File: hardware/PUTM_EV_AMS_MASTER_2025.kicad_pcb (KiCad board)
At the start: 4 copper layers, 60 x 100 mm, 261 parts, among them IC1 TPS7B92033DBVR, IC11 ISO6760, IC2 TPS54202HDDCR, IC3 BQ79600PWRQ1, IC4 ADS131M04, IC5 LTC1799, IC6 LTC6820IMS, IC7 ISO6760, IC8 3.3V/0.5A, J1 M80-5100642, J10 M300-MV10345M1, J12 M80-51034XX, J2 USB_C_Receptacle_USB2.0_14P, J3 M80-51014XX, J4 FTSH-107-01-L-D-K, J5 M80-51004XX, J7 M300-MV10345M1, J8 M80-51004XX, K1 IMB03ITS, Q1 DMT6018LDR-7, Q2 DMT6018LDR-7, Q3 DMT6018LDR-7, Q4 DMT6018LDR-7, Q5 DMT6018LDR-7, Q6 2N7002, Q7 DMT6018LDR-7, Q8 2N7002, Q9 2N7002, T1 >100kHz, U1 MCP2542FD-E/MF, U10 STM32G484VEHx, U11 LM397, U12 LMR33640DDDA, U2 LM397, U3 74AUP1G32, U4 UCC12040DVE, U5 LM397, U6 MCP2542FD-E/MF, U7 MCP2542FD-E/MF, U8 LM397, U9 LM397, Y1 X322516MLB4SI

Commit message: sync
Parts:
- removed C76: 10nF, Capacitor_SMD:C_0603_1608Metric
- removed C77: 100nF, Capacitor_SMD:C_0603_1608Metric
- removed R84, R85, R86, R87: 10k, Resistor_SMD:R_0603_1608Metric
- removed R88, R89, R90: TBD, Resistor_SMD:R_0603_1608Metric
- removed U11: LM397, Package_TO_SOT_SMD:SOT-23-5
- added C81: 100nF, Capacitor_SMD:C_0603_1608Metric, F.Cu at (191.2, 34.4)
- added C82: 100nF, Capacitor_SMD:C_0603_1608Metric, F.Cu at (191.2, 36.9)
- added R100: 100, Resistor_SMD:R_0603_1608Metric, F.Cu at (202.3, 34.4)
- added R101: 10k, Resistor_SMD:R_0603_1608Metric, F.Cu at (191.2, 39.4)
- added R102: 10k, Resistor_SMD:R_0603_1608Metric, F.Cu at (191.2, 42.0)
- added R103: 10k, Resistor_SMD:R_0603_1608Metric, F.Cu at (191.2, 44.5)
- added R104: 10k, Resistor_SMD:R_0603_1608Metric, F.Cu at (191.2, 47.0)
- added R105: TBD, Resistor_SMD:R_0603_1608Metric, F.Cu at (191.2, 49.5)
- added R106: TBD, Resistor_SMD:R_0603_1608Metric, F.Cu at (191.2, 52.0)
- added R107: TBD, Resistor_SMD:R_0603_1608Metric, F.Cu at (191.2, 54.5)
- added U13: LM397, Package_TO_SOT_SMD:SOT-23-5, F.Cu at (195.8, 35.6)
- C5, C72, C74: value 10nF -> 100nF
- IC4: value ADS131M04 -> ~
- R38: value 10k -> TBD
- R42: value TBD -> 10k
- moved C74 10.1 mm to (181.5, 116.5)
- moved C75 10.1 mm to (178.5, 121.0)
- moved R77 10.1 mm to (178.5, 116.5)
- moved R78 10.1 mm to (178.5, 119.5)
- moved R79 10.1 mm to (178.5, 115.0)
- moved R80 10.1 mm to (178.5, 118.0)
- moved R81 10.1 mm to (181.5, 118.0)
- moved R82 10.1 mm to (181.5, 119.5)
- moved R83 10.1 mm to (181.5, 121.0)
- moved U9 10.1 mm to (180.0, 118.0)
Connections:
- net /Connectivity/EAAE renamed /Connectivity/AIR Minus/EI1
- net /Connectivity/EAAM renamed /Connectivity/AIR Plus/EI1
- C5 pad 1: /Connectivity/EI2 -> /Connectivity/Input2/EI1
- C50 pad 1: /Connectivity/EI1 -> +24V
- C66 pad 1: +24V -> /Connectivity/AIR Precharge/EI1
- Q6 pad 1: /MCU/SIGNAL_AMS_ERROR -> Net-(Q6-G)
- R11 pad 1: /MCU/SIGNAL_AMS_ERROR -> Net-(Q6-G)
- R33 pad 1: /Connectivity/EI2 -> +24V
- R33 pad 2: /CHARGER_DETECTION -> /Connectivity/Input2/EI1
- R35 pad 1: /Connectivity/EI2 -> /Connectivity/Input2/EI1
- R38 pad 1: +3.3V -> /Connectivity/Input2/EI1
- R38 pad 2: /Connectivity/UC_IN1 -> /CHARGER_DETECTION
- R39 pad 1: Net-(R39-Pad1) -> +3.3V
- R39 pad 2: /Connectivity/UC_IN1 -> /AIR_PRE_DETECTION
- R40 pad 1: +3.3V -> Net-(R40-Pad1)
- R40 pad 2: Net-(R39-Pad1) -> /AIR_PRE_DETECTION
- R41 pad 1: Net-(R39-Pad1) -> +3.3V
- R41 pad 2: GND -> Net-(R40-Pad1)
- R42 pad 1: /Connectivity/EI1 -> Net-(R40-Pad1)
- R42 pad 2: TSMS -> GND
- R43 pad 1: /Connectivity/EI1 -> +24V
- R43 pad 2: GND -> /Connectivity/AIR Precharge/EI1
- R68 pad 1: +24V -> /Connectivity/AIR Precharge/EI1
- R68 pad 2: /Connectivity/EI1 -> GND
- R69 pad 1: +24V -> /Connectivity/AIR Precharge/EI1
- R69 pad 2: /Connectivity/EI2 -> /Connectivity/EX_AIR_AUX_PRE
- R70 pad 2: /AIR_PRE_DETECTION -> /Connectivity/UC_AIR_AUX_M
- R71 pad 2: /AIR_PRE_DETECTION -> /Connectivity/UC_AIR_AUX_M
- R76 pad 2: /Connectivity/EX_AIR_AUX_PRE -> /AIR_M_DETECTION
- R77 pad 2: /Connectivity/UC_AIR_AUX_M -> /Connectivity/UC_AIR_AUX_P
- R78 pad 2: /Connectivity/UC_AIR_AUX_M -> /Connectivity/UC_AIR_AUX_P
- R83 pad 2: /AIR_M_DETECTION -> /AIR_P_DETECTION
- U2 pad 3: /Connectivity/EI2 -> /Connectivity/Input2/EI1
- U5 pad 1: Net-(R39-Pad1) -> Net-(R40-Pad1)
- U5 pad 3: /Connectivity/EI1 -> /Connectivity/AIR Precharge/EI1
- U5 pad 4: /Connectivity/UC_IN1 -> /AIR_PRE_DETECTION
- U8 pad 4: /AIR_PRE_DETECTION -> /Connectivity/UC_AIR_AUX_M
- U9 pad 4: /Connectivity/UC_AIR_AUX_M -> /Connectivity/UC_AIR_AUX_P
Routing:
- net (no net): track 0.00 -> 29.1 mm
- net +24V: track 12.7 -> 4.34 mm, vias 5 -> 0
- net Net-(R39-Pad1): track 7.43 -> 0.00 mm, vias 1 -> 0
- net Net-(R85-Pad1): track 7.43 -> 0.00 mm, vias 1 -> 0
- net /Connectivity/EI1: track 6.79 -> 0.00 mm, vias 1 -> 0
- net /Connectivity/EI2: track 6.79 -> 0.00 mm, vias 1 -> 0
- net /Connectivity/EAAP: track 6.79 -> 0.00 mm, vias 1 -> 0
- net /AIR_PRE_DETECTION: track 4.78 -> 0.00 mm, vias 1 -> 0
- net /Connectivity/UC_AIR_AUX_P: track 4.78 -> 7.37 mm, vias 1 -> 0
- net /Connectivity/AIR Plus/EI1: track 6.79 -> 5.57 mm, vias 1 -> 0
- net /Connectivity/AIR Minus/EI1: track 6.79 -> 5.57 mm, vias 1 -> 0
- net Net-(R78-Pad1): track 7.43 -> 6.21 mm, vias 1 -> 0
- net Net-(R71-Pad1): track 7.43 -> 6.21 mm, vias 1 -> 0
- net Net-(R17-Pad1): track 7.43 -> 6.21 mm, vias 1 -> 0
- net /Connectivity/UC_IN2: track 4.78 -> 3.68 mm, vias 1 -> 0
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
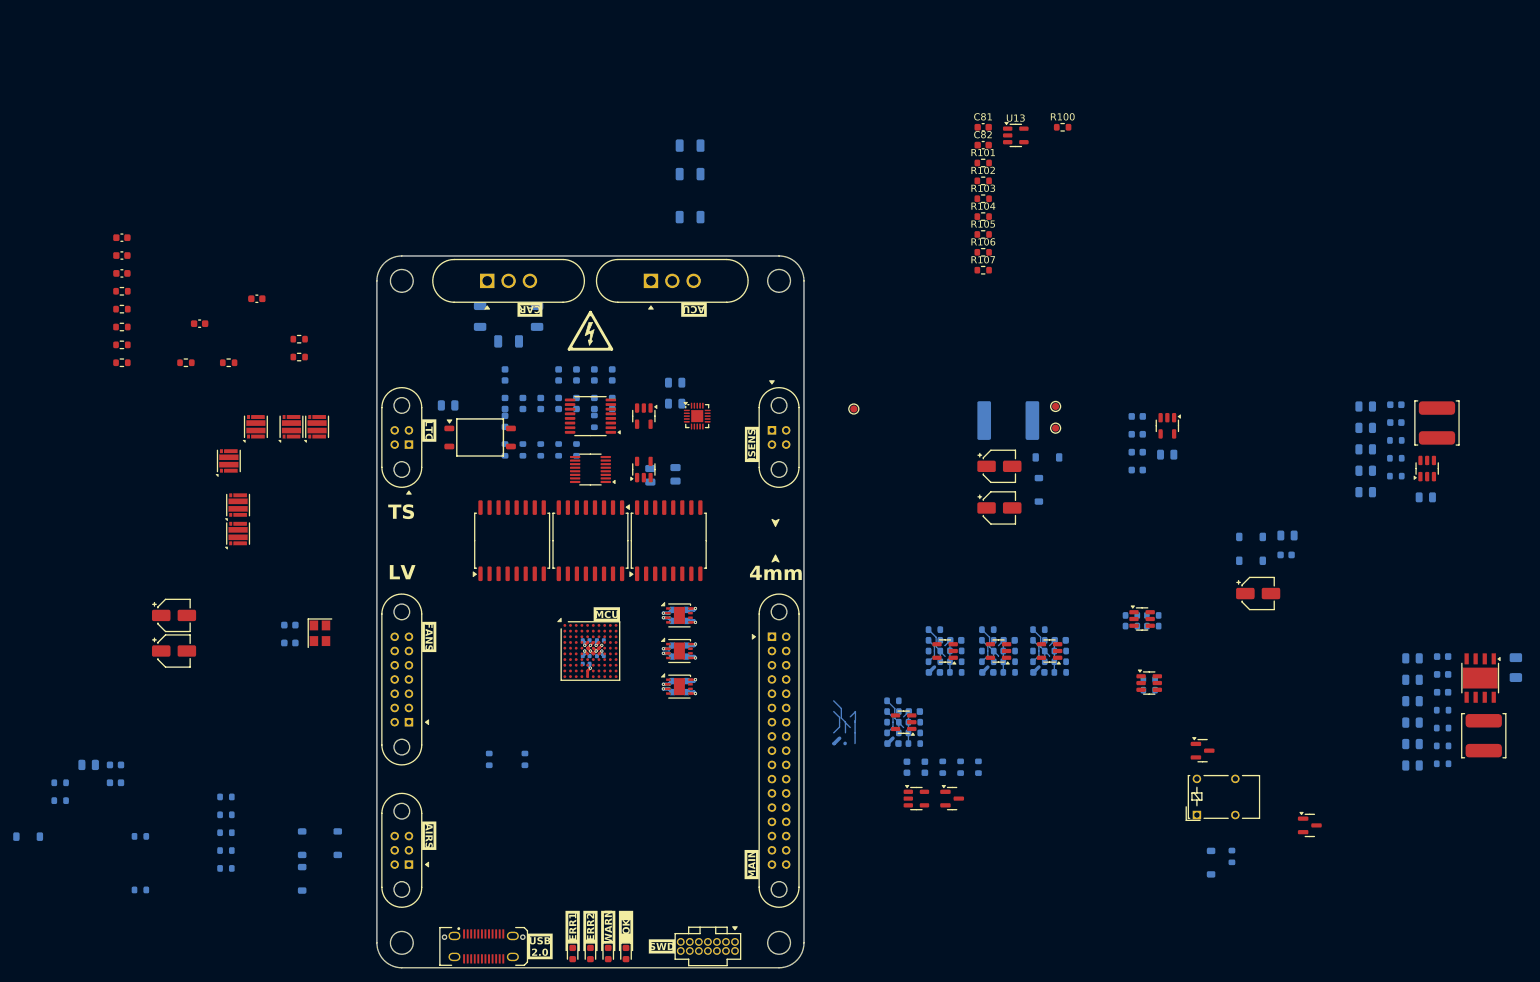
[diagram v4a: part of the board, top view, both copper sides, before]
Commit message: the connectors wil stay and wont be changed further
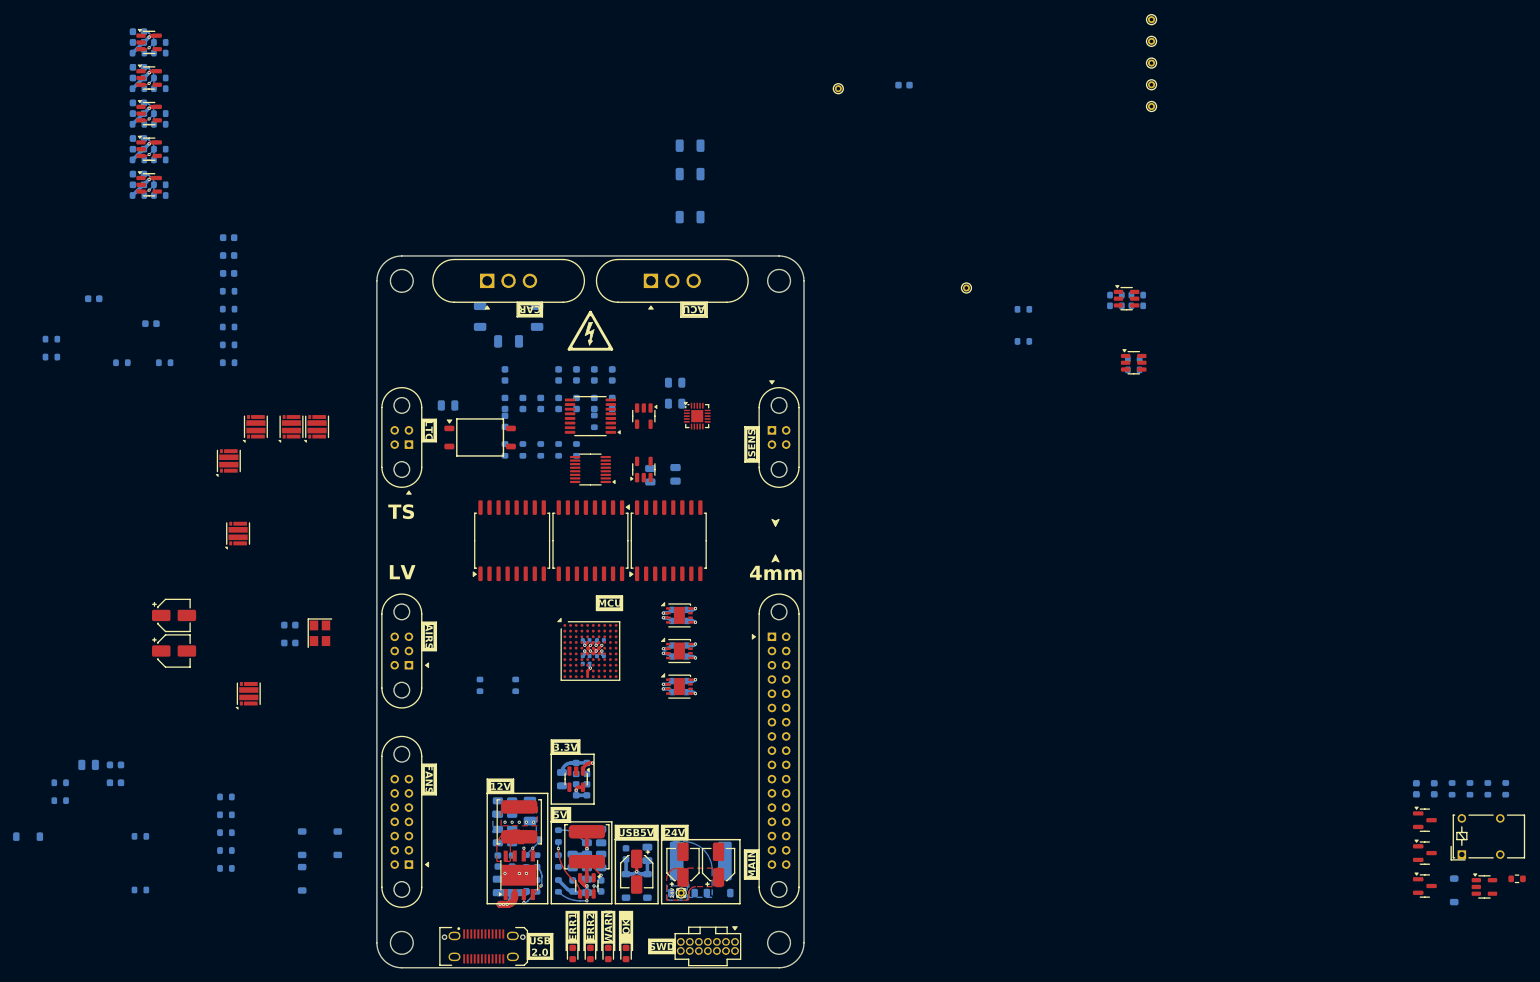
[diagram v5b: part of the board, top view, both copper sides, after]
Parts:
- removed R101, R102, R103, R104, R15, R32, R39, R40, R41, R42, R70, R71, R72, R73, R77, R78, R79, R80: 10k, Resistor_SMD:R_0603_1608Metric
- added C76: 100nF, Capacitor_SMD:C_0603_1608Metric, B.Cu at (180.1, 28.5)
- added TP4: TestPoint_Small, TestPoint:TestPoint_THTPad_D1.0mm_Drill0.5mm, F.Cu at (214.8, 19.3)
- added TP5: TestPoint_Small, TestPoint:TestPoint_THTPad_D1.0mm_Drill0.5mm, F.Cu at (214.8, 22.4)
- added TP6: TestPoint_Small, TestPoint:TestPoint_THTPad_D1.0mm_Drill0.5mm, F.Cu at (214.8, 25.4)
- added TP7: TestPoint_Small, TestPoint:TestPoint_THTPad_D1.0mm_Drill0.5mm, F.Cu at (214.8, 28.4)
- added TP8: TestPoint_Small, TestPoint:TestPoint_THTPad_D1.0mm_Drill0.5mm, F.Cu at (214.8, 31.5)
- C43, C53, C78, C79, C80, C82, R105, R106, R107, R91, R92, R93, R94, R95, R96, R97, R98, R99: moved to B.Cu
- C5, C66, C72, C74: value 100nF -> TBD
- C81: value 100nF -> TBD; moved to B.Cu
- TP1, TP2, TP3: footprint TestPoint:TestPoint_Pad_D1.0mm -> TestPoint:TestPoint_THTPad_D1.0mm_Drill0.5mm
- moved C66 155.2 mm to (72.5, 21.0), turned to 180 degrees
- moved R69 152.7 mm to (75.5, 22.5), turned to 0 degrees
- moved R33 150.7 mm to (72.5, 34.0)
- moved C5 149.9 mm to (72.5, 31.0), turned to 180 degrees
- moved R43 149.2 mm to (72.5, 24.0)
- moved C71 148.6 mm to (72.5, 22.5), turned to 180 degrees
- moved R35 147.3 mm to (75.5, 34.0)
- moved U2 147.3 mm to (74.0, 32.5), turned to 0 degrees
- moved U5 146.8 mm to (74.0, 22.5), turned to 0 degrees
- moved R68 145.9 mm to (75.5, 24.0), turned to 0 degrees
- moved C50 143.0 mm to (72.5, 32.5), turned to 180 degrees
- moved F3 140.0 mm to (127.5, 130.5)
- moved R38 137.9 mm to (75.5, 32.5), turned to 0 degrees
- moved U12 137.8 mm to (126.0, 139.5), turned to 90 degrees
- moved L2 136.0 mm to (126.0, 132.0), turned to 90 degrees
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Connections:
- net Net-(D16-K) renamed /Power/F_24V
- net Net-(IC2-BOOT) renamed /Power/BOOT_5V
- net Net-(IC2-EN) renamed /Power/EN_5V
- net Net-(IC2-FB) renamed /Power/FB_5V
- net Net-(U12-BOOT) renamed /Power/BOOT_12V
- net Net-(U12-FB) renamed /Power/FB_12V
- net Net-(U12-VCC) renamed /Power/VCC_12V
- J12 pad 10: /CHARGER_DETECTION -> /SAFETY1
- J12 pad 11: unconnected-(J12-Pin_11-Pad11) -> /SAFETY2
- J12 pad 12: /AIR_PRE_DETECTION -> /EXT_SCK
- J12 pad 13: /AIR_M_DETECTION -> /EXT_MOSI
- J12 pad 14: /AIR_P_DETECTION -> /EXT_MISO
- J12 pad 15: unconnected-(J12-Pin_15-Pad15) -> /~{EXT_CS}
- J12 pad 16: /D- -> VDD
- J12 pad 17: /D+ -> GND
- J12 pad 19: VDD -> unconnected-(J12-Pin_19-Pad19)
- J12 pad 2: VDD -> unconnected-(J12-Pin_2-Pad2)
- J12 pad 20: GND -> /CHARGER_DETECTION
- J12 pad 22: /CANFD3- -> /AIR_PRE_DETECTION
- J12 pad 23: /CANFD3+ -> /AIR_M_DETECTION
- J12 pad 24: /CANFD2- -> /AIR_P_DETECTION
- J12 pad 25: /CANFD2+ -> unconnected-(J12-Pin_25-Pad25)
- J12 pad 26: /CANFD1- -> unconnected-(J12-Pin_26-Pad26)
- J12 pad 27: /CANFD1+ -> unconnected-(J12-Pin_27-Pad27)
- J12 pad 3: GND -> /CANFD3+
- J12 pad 31: /EXT_SCK -> /D-
- J12 pad 32: /EXT_MOSI -> /D+
- J12 pad 33: /EXT_MISO -> VDD
- J12 pad 34: /~{EXT_CS} -> GND
- J12 pad 4: unconnected-(J12-Pin_4-Pad4) -> /CANFD3-
- J12 pad 5: /SAFETY1 -> /CANFD2+
- J12 pad 6: /SAFETY2 -> /CANFD2-
- J12 pad 7: unconnected-(J12-Pin_7-Pad7) -> /CANFD1+
- J12 pad 8: unconnected-(J12-Pin_8-Pad8) -> /CANFD1-
- R17 pad 1: Net-(R17-Pad1) -> +3.3V
- R17 pad 2: /Connectivity/UC_IN2 -> /Connectivity/AIR Minus/REF
- R26 pad 1: +3.3V -> /Connectivity/AIR Minus/REF
- R26 pad 2: Net-(R17-Pad1) -> GND
- U13 pad 1: Net-(R102-Pad1) -> /Connectivity/AIR Minus/REF
- U2 pad 1: Net-(R17-Pad1) -> /Connectivity/AIR Minus/REF
- U5 pad 1: Net-(R40-Pad1) -> /Connectivity/AIR Minus/REF
- U8 pad 1: Net-(R71-Pad1) -> /Connectivity/AIR Minus/REF
- U9 pad 1: Net-(R78-Pad1) -> /Connectivity/AIR Minus/REF
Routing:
- net +24V: track 4.34 -> 40.1 mm, vias 0 -> 13
- net (no net): track 29.1 -> 0.00 mm
- net /Power/F_5V: track 0.00 -> 10.8 mm, vias 0 -> 1
- net /Power/FB_5V: track 0.00 -> 9.11 mm, vias 0 -> 1
- net Net-(D14-K): track 0.00 -> 8.96 mm, vias 0 -> 1
- net /Connectivity/UC_AIR_AUX_P: track 7.37 -> 0.00 mm
- net /Connectivity/Input1/EI1: track 0.00 -> 7.36 mm, vias 0 -> 1
- net /Connectivity/Input2/EI1: track 0.00 -> 7.36 mm, vias 0 -> 1
- net /Power/F_+3.3V: track 0.00 -> 6.96 mm, vias 0 -> 1
- net /Connectivity/AIR Precharge/EI1: track 1.09 -> 7.36 mm, vias 0 -> 1
- net Net-(R71-Pad1): track 6.21 -> 0.00 mm
- net Net-(R78-Pad1): track 6.21 -> 0.00 mm
- net Net-(R17-Pad1): track 6.21 -> 0.00 mm
- net /Power/SW_5V: track 0.00 -> 5.76 mm, vias 0 -> 1
- net /Power/EN_5V: track 0.00 -> 5.28 mm, vias 0 -> 1
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- added copper zone on B.Cu, net +24V
- added copper zone on F.Cu, net +24V
- added copper zone on B.Cu, net /Power/F_12V
- added copper zone on F.Cu, net /Power/F_12V
- added copper zone on B.Cu, net /Power/F_24V
- added copper zone on F.Cu, net /Power/SW_12V
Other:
- board text added: "12V"
- board text added: "24V"
- board text added: "3.3V"
- board text added: "5V"
- board text added: "USB5V"

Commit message: LV section component placement done
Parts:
- removed D22: VSSB410S-E3/52T, Diode_SMD:D_SOD-123
- added D13: VSSB410S-E3/52T, Diode_SMD:D_SOD-123, F.Cu at (120.0, 134.5)
- added R15: 100, Resistor_SMD:R_0603_1608Metric, B.Cu at (145.5, 126.0)
- added R32: 100, Resistor_SMD:R_0603_1608Metric, B.Cu at (141.5, 129.5)
- added TP10: TestPoint_Small, TestPoint:TestPoint_THTPad_D1.0mm_Drill0.5mm, F.Cu at (131.5, 134.8)
- added TP9: TestPoint_Small, TestPoint:TestPoint_THTPad_D1.0mm_Drill0.5mm, F.Cu at (123.2, 124.2)
- D15, D17, D21, D24, D8, D9: moved to F.Cu
- R100: moved to B.Cu
- moved C53 137.1 mm to (202.8, 71.0)
- moved C43 128.7 mm to (202.8, 68.5)
- moved R94 127.3 mm to (202.8, 81.0)
- moved R100 125.9 mm to (141.5, 122.5), turned to -90 degrees
- moved R95 122.1 mm to (206.8, 68.5)
- moved R96 122.1 mm to (206.8, 71.0)
- moved R97 122.1 mm to (206.8, 73.5)
- moved R98 122.1 mm to (206.8, 76.0)
- moved R99 122.1 mm to (206.8, 78.5)
- moved C78 119.9 mm to (202.8, 73.5)
- moved C79 119.9 mm to (202.8, 76.0)
- moved C80 119.9 mm to (202.8, 78.5)
- moved R14 119.2 mm to (145.5, 122.5)
- moved U3 116.9 mm to (146.0, 123.5), turned to -90 degrees
- moved R13 116.6 mm to (145.5, 129.5)
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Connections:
- net Net-(Q2A-G1) renamed /Fan Control/G1
- net Net-(Q2B-G2) renamed /Fan Control/G2
- net Net-(Q3A-G1) renamed /Fan Control/G3
- net Net-(Q3B-G2) renamed /Fan Control/G4
- net Net-(Q4A-G1) renamed /Fan Control/G5
- net Net-(Q4B-G2) renamed /Fan Control/G6
- net Net-(Q5A-G1) renamed /Fan Control/G7
- net Net-(Q7A-G1) renamed /AIR Control/G1
- D17 pad 2: /Fan Control/FAN2_DRAIN -> /FAN5-
- D18 pad 2: /Fan Control/FAN3_DRAIN -> /FAN2-
- D19 pad 2: /Fan Control/FAN4_DRAIN -> /FAN4-
- D20 pad 2: /Fan Control/FAN5_DRAIN -> /FAN6-
- D21 pad 2: /Fan Control/FAN6_DRAIN -> /FAN7-
- D8 pad 2: /Fan Control/FAN1_DRAIN -> /FAN1-
- J12 pad 16: VDD -> GND
- J12 pad 17: GND -> VDD
- J12 pad 33: VDD -> GND
- J12 pad 34: GND -> VDD
- Q1 pad 1: Net-(Q1A-G1) -> /AIR Control/G2
- Q2 pad 5: /Fan Control/FAN1_DRAIN -> /FAN1-
- Q2 pad 6: /Fan Control/FAN2_DRAIN -> /FAN2-
- Q3 pad 5: /Fan Control/FAN3_DRAIN -> /FAN3-
- Q3 pad 6: /Fan Control/FAN4_DRAIN -> /FAN4-
- Q4 pad 5: /Fan Control/FAN5_DRAIN -> /FAN5-
- Q4 pad 6: /Fan Control/FAN6_DRAIN -> /FAN6-
- Q5 pad 5: /Fan Control/FAN7_DRAIN -> /FAN7-
- Q7 pad 4: Net-(Q7B-G2) -> /AIR Control/G2
- Q8 pad 1: /MCU/DETECT_WTDG -> Net-(Q8-G)
- Q9 pad 1: /AMS_ERROR -> /Safety/AMS_OK
- R13 pad 1: /AMS_ERROR -> /Safety/AMS_OK
- R37 pad 2: Net-(Q7B-G2) -> /AIR Control/G2
- R45 pad 2: Net-(Q1A-G1) -> /AIR Control/G2
- R46 pad 2: Net-(Q7B-G2) -> /AIR Control/G2
- R48 pad 2: Net-(Q1A-G1) -> /AIR Control/G2
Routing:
- net /Connectivity/AIR Minus/REF: track 0.00 -> 31.9 mm, vias 0 -> 1
- net /Safety/CAP_VOLT: track 0.00 -> 14.1 mm, vias 0 -> 1
- net /Safety/RELAY-: track 0.00 -> 12.6 mm, vias 0 -> 1
- net /SAFETY1: track 0.00 -> 12.5 mm
- net /AIR Control/G2: track 0.00 -> 11.0 mm, vias 0 -> 2
- net +24V: track 40.1 -> 48.9 mm
- net +5V: track 9.66 -> 18.1 mm
- net /MCU/CLK_OUT: track 0.00 -> 7.86 mm, vias 0 -> 1
- net /SAFETY2: track 0.00 -> 7.12 mm
- net +3.3V: track 6.00 -> 12.6 mm, vias 3 -> 5
- net /Fan Control/G7: track 0.00 -> 5.52 mm, vias 0 -> 1
- net /Fan Control/G6: track 0.00 -> 5.52 mm, vias 0 -> 1
- net /AIR Control/G1: track 0.00 -> 5.52 mm, vias 0 -> 1
- net /Fan Control/G5: track 0.00 -> 5.52 mm, vias 0 -> 1
- net /Fan Control/G4: track 0.00 -> 5.52 mm, vias 0 -> 1
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- added copper zone on B.Cu, net /TSMS_AIRS
- added copper zone on F.Cu, net /TSMS_AIRS
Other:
- board text added: "AIR CR"
- board text added: "CAN"
- board text added: "FAN CR"
- board text added: "IN SEP"
- board text added: "LEDS"
- board text added: "SAFETY"
- board text added: "TSMS"
- board text added: "USB"

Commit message: sync
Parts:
- added C77: 22uF, Capacitor_SMD:C_0805_2012Metric, F.Cu at (174.6, 84.0)
- added TP11: TestPoint_Small, TestPoint:TestPoint_THTPad_D1.0mm_Drill0.5mm, F.Cu at (123.5, 116.0)
- added TP12: TestPoint_Small, TestPoint:TestPoint_THTPad_D1.0mm_Drill0.5mm, F.Cu at (131.8, 110.0)
- added TP13: TestPoint_Small, TestPoint:TestPoint_THTPad_D1.0mm_Drill0.5mm, F.Cu at (131.8, 119.0)
- added TP14: TestPoint_Small, TestPoint:TestPoint_THTPad_D1.0mm_Drill0.5mm, F.Cu at (131.8, 114.5)
- added TP15: TestPoint_Small, TestPoint:TestPoint_THTPad_D1.0mm_Drill0.5mm, F.Cu at (131.8, 105.5)
- added TP16: TestPoint_Small, TestPoint:TestPoint_THTPad_D1.0mm_Drill0.5mm, F.Cu at (131.8, 123.5)
- added TP17: TestPoint_Small, TestPoint:TestPoint_THTPad_D1.0mm_Drill0.5mm, F.Cu at (148.2, 128.5)
- added TP18: TestPoint_Small, TestPoint:TestPoint_THTPad_D1.0mm_Drill0.5mm, F.Cu at (148.2, 123.5)
- moved C40 58.0 mm to (124.0, 87.5), turned to 0 degrees
- moved C39 45.2 mm to (143.5, 97.5), turned to 0 degrees
- moved C44 42.5 mm to (143.5, 87.5), turned to 0 degrees
- moved C46 41.0 mm to (139.5, 87.5), turned to 180 degrees
- moved C45 38.7 mm to (139.5, 97.5), turned to 180 degrees
- moved C59 29.7 mm to (124.0, 97.5), turned to 0 degrees
- moved C72 13.5 mm to (134.3, 103.0)
- moved C73 13.5 mm to (134.2, 104.5)
- moved R74 13.5 mm to (134.2, 106.0)
- moved R75 13.5 mm to (137.2, 106.0)
- moved R76 13.5 mm to (137.2, 104.5)
- moved U8 13.5 mm to (135.8, 104.5)
- moved C66 9.03 mm to (134.3, 112.0)
- moved C71 9.03 mm to (134.2, 113.5)
- moved R43 9.03 mm to (134.2, 115.0)
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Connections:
- net /SAFETY1 renamed /SAFETY_IN
- net /SAFETY2 renamed /SAFETY_OUT
- R69 pad 2: /Connectivity/EX_AIR_AUX_PRE -> /AIR_PRE_DETECTION
- U10 pad A7: /Connectivity/EX_AIR_AUX_PRE -> /Connectivity/UC_AIR_AUX_PRE
- U5 pad 4: /AIR_PRE_DETECTION -> /Connectivity/UC_AIR_AUX_PRE
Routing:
- net +3.3V: track 12.6 -> 103.1 mm, vias 5 -> 7
- net +12V: track 0.00 -> 43.4 mm, vias 0 -> 4
- net /Connectivity/UC_AIR_AUX_P: track 0.00 -> 25.4 mm
- net /Connectivity/UC_IN2: track 0.00 -> 22.2 mm
- net /Connectivity/UC_AIR_AUX_PRE: track 0.00 -> 17.0 mm
- net /Connectivity/AIR Minus/REF: track 31.9 -> 46.8 mm
- net +3.3VIO: track 7.48 -> 22.1 mm
- net /Connectivity/UC_IN1: track 0.00 -> 13.8 mm
- net /CANFD3+: track 0.00 -> 11.6 mm
- net /CANFD3-: track 0.00 -> 11.6 mm
- net /CANFD2-: track 0.00 -> 11.3 mm
- net /CANFD2+: track 0.00 -> 11.3 mm
- net /CANFD1-: track 0.00 -> 11.1 mm
- net /CANFD1+: track 0.00 -> 11.1 mm
- net /Connectivity/UC_AIR_AUX_M: track 0.00 -> 10.2 mm
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- added copper zone on B.Cu, net +12V
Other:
- board text added: "AM"
- board text added: "AP"
- board text added: "APRE"
- board text added: "IN"
- board text added: "IN1"
- board text added: "IN2"
- board text added: "ISO"
- board text added: "OUT"
